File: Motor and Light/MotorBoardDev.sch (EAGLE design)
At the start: 79 parts, among them IC1 74HC04D, J1 Under Glow, J2 Safety Light, J3 12V, J4 24V, Q1 BC846ASMD, Q2 220mA/50V/3.5Ω, Q7 220mA/50V/3.5Ω, Q8 220mA/50V/3.5Ω, Q9 220mA/50V/3.5Ω, T11 TIP41A, T12 TIP41A, T13 TIP41A, T14 TIP41A, T15 TIP41A, T16 TIP41A, T17 TIP41A, T18 TIP41A, T19 TIP41A, T2 TIP41A, U2 9DoF IMU, X1 C-GRID-05-15-91, X2 C-GRID-05-15-91, X4 C-GRID-02-70553, X5 SI-50170, X7 2510-, X8 2510-

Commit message: added mbed pin maps
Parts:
- added R39, R40: 150, rcl:R-US_R0603
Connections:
- removed net VCC: X1-4.S, X2-4.S
- new net N$37: R39.1, U$15.P$30
- new net N$38: R40.1, U$15.P$29
- net +3V3: now also U2.!CS
- net +5V: now also X1-4.S, X2-4.S
- net 1S1: now also U$15.P$28
- net 1S2: now also U$15.P$27
- net 1S3: now also U$15.P$26
- net 2S1: now also U$15.P$5
- net 2S2: now also U$15.P$6
- net 2S3: now also U$15.P$7
- net BATTIN: now also U$15.P$20
- net ETH_LED1: now also R39.2
- net ETH_LED2: now also R40.2
- net GND: now also U2.FSYNC
- net GYRO_INT: now also U$15.P$14
- net LDIR: now also U$15.P$17
- net LEA3: now also U$15.P$24
- net LEB3: now also U$15.P$23
- net LSPEED: now also U$15.P$18
- net RDIR: now also U$15.P$15
- net REA3: now also U$15.P$22
- net REB3: now also U$15.P$21
- net RSPEED: now also U$15.P$16
- net SLIGHT: now also U$15.P$25

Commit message: added regulators
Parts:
- added C11, C12, C13, C14: (no value), rcl:C-USC0805
- added C6: 0.1uF, rcl:C-USC0603
- added U$7: NCP1117DT50GOS-ND, IGVC-Regulators:NCP1117DT50GOS-ND
- added U$8: NCP1117DT33GOS-ND, IGVC-Regulators:NCP1117DT33GOS-ND
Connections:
- net +12V: now also C11.1, C13.1, U$7.IN, U$8.IN
- net +3V3: now also C14.1, U$8.OUT
- net +5V: now also C12.1, C6.1, U$15.P$2, U$7.OUT
- net GND: now also C11.2, C12.2, C13.2, C14.2, C6.2, U$7.GND, U$8.GND

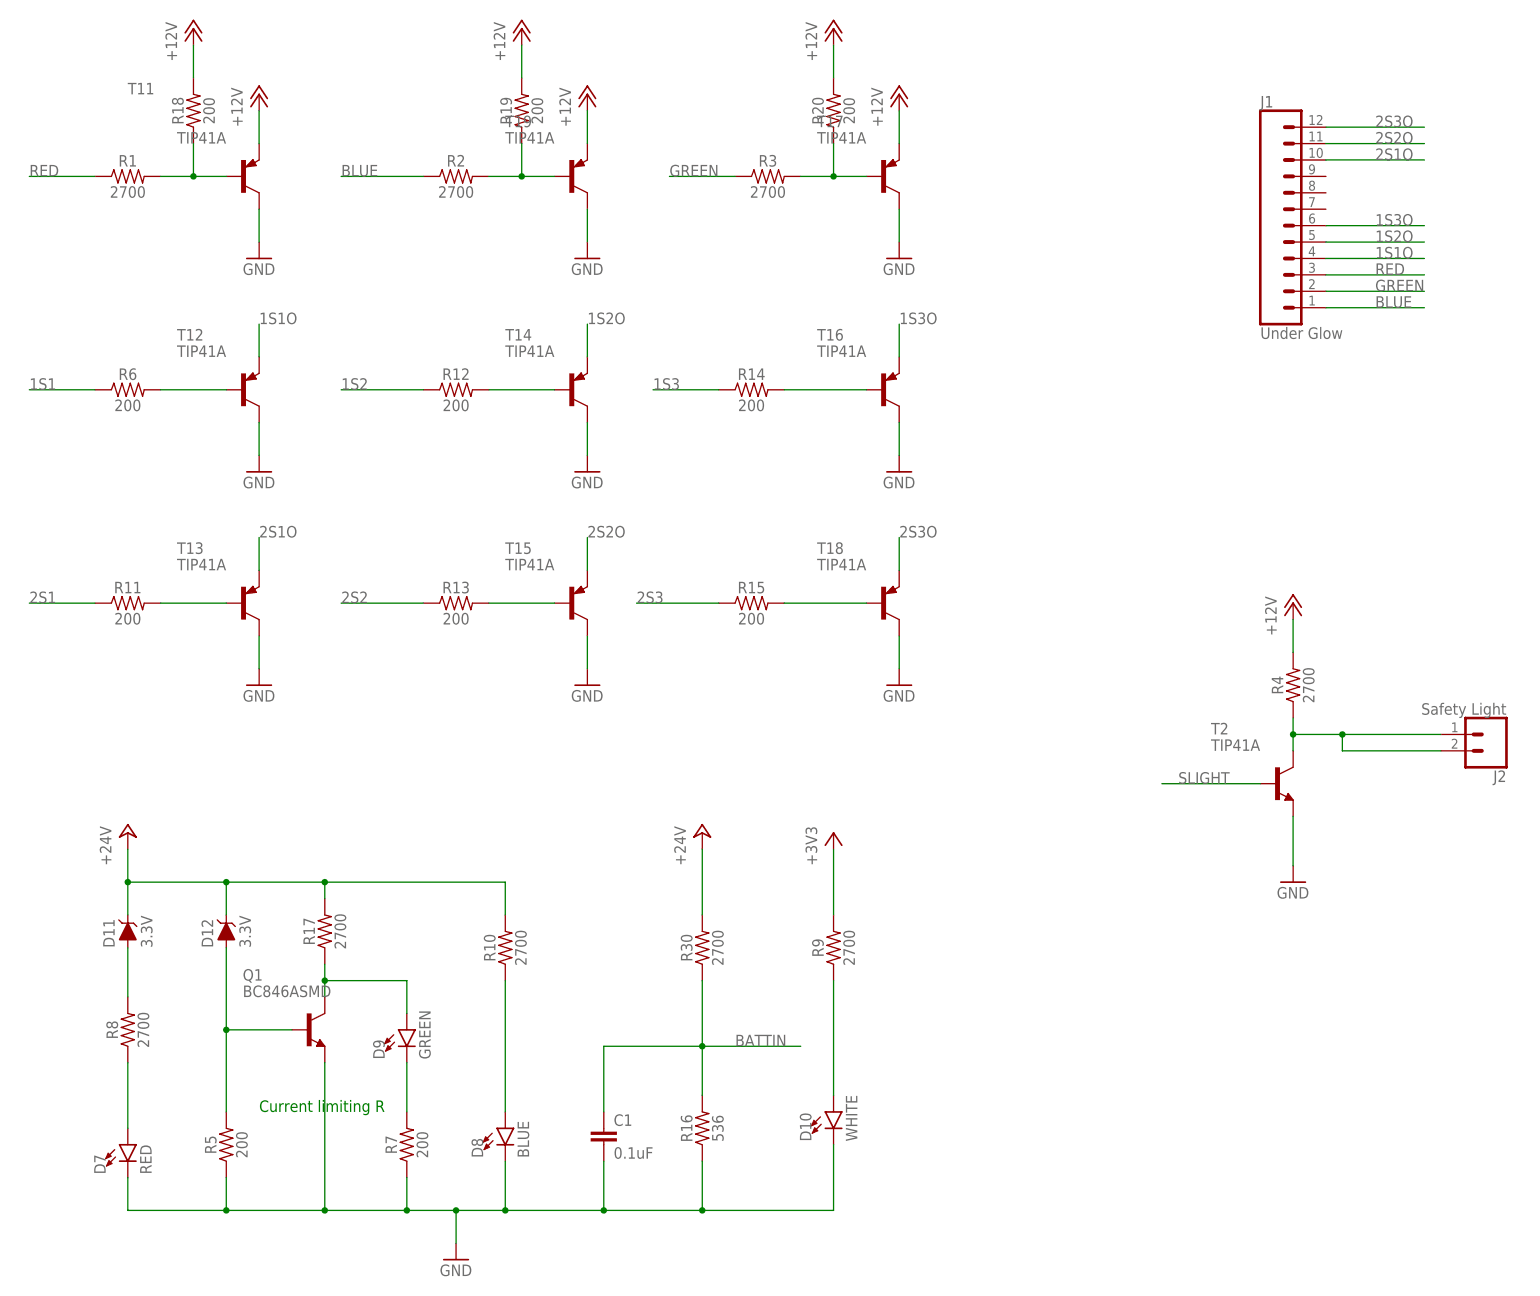
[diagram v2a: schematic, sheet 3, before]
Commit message: Schematics Updated, Layout initial commit
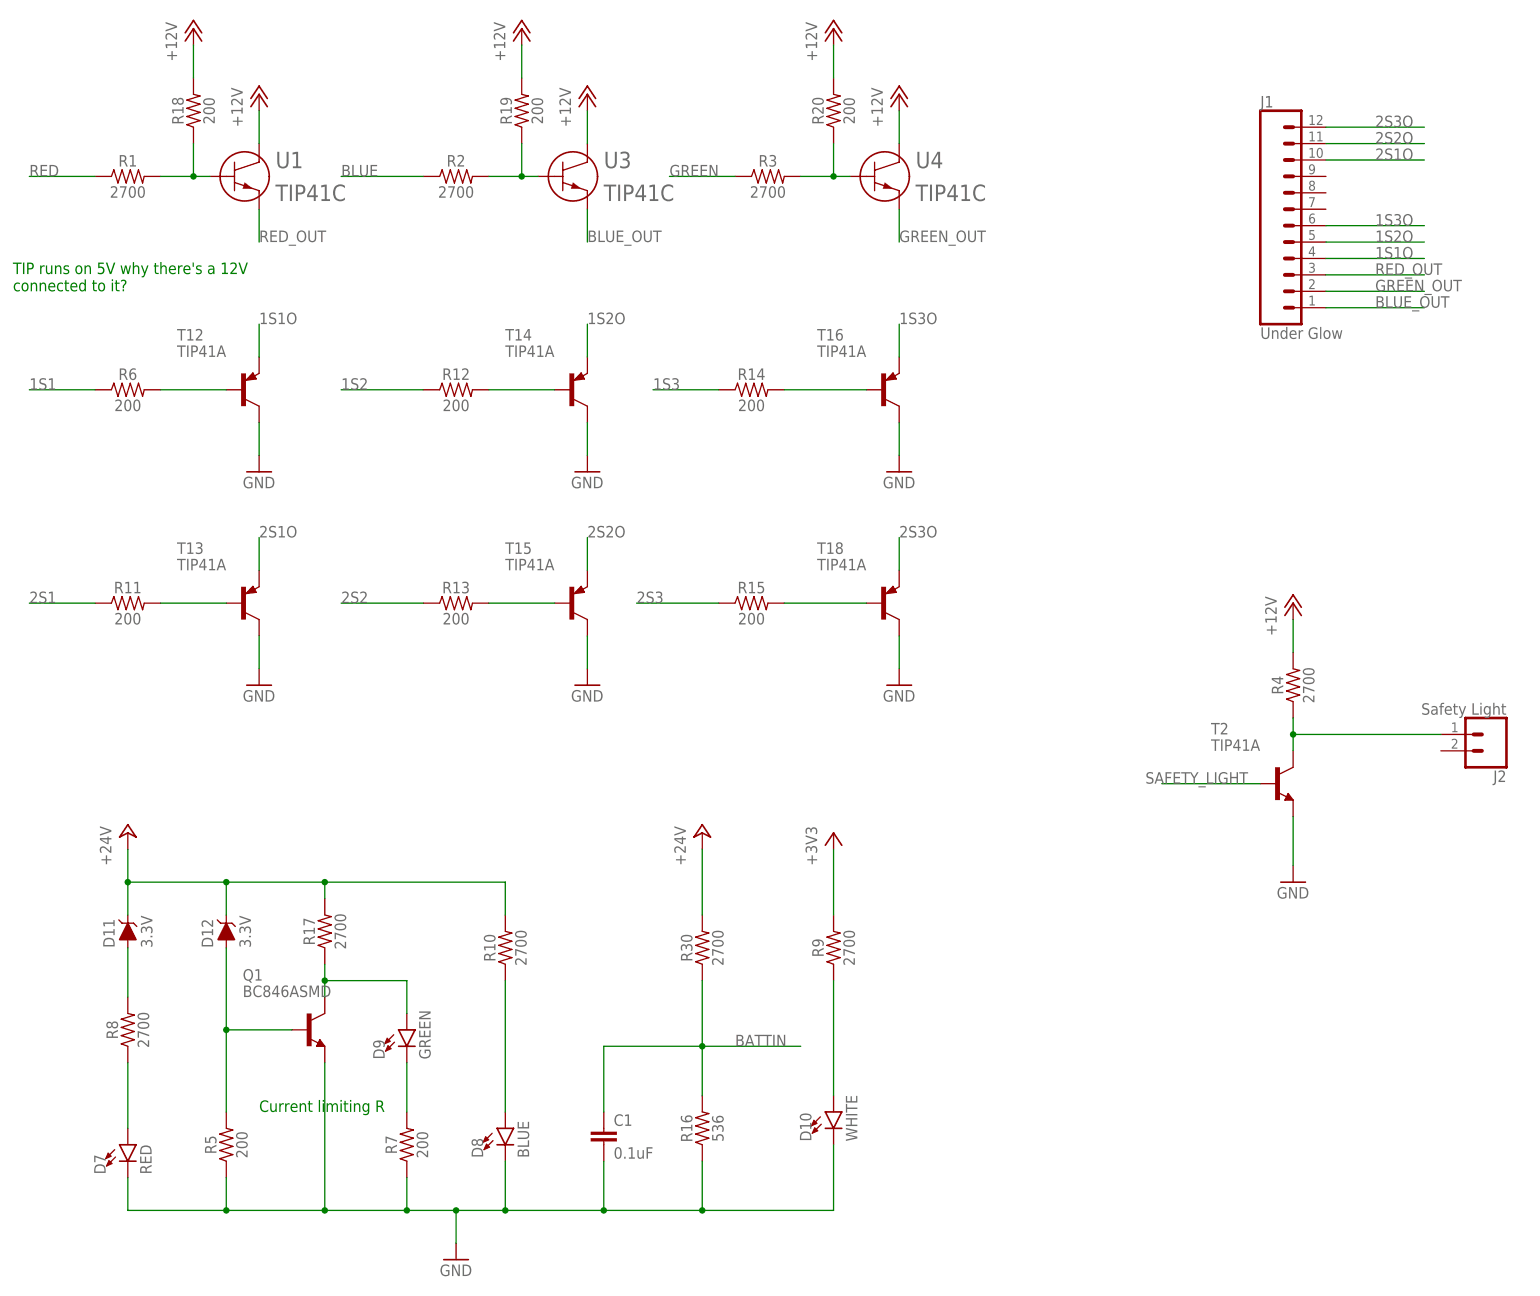
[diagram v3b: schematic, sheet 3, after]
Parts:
- removed T11, T17, T19: TIP41A, transistor:-PNP-TO220V
- added U1, U3, U4: TIP41C, DigiKey:TIP41C
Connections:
- net SLIGHT renamed SAFETY_LIGHT
- new net BLUE_OUT: J1.1, U3.E3
- new net GREEN_OUT: J1.2, U4.E3
- new net RED_OUT: J1.3, U1.E3
- net +12V: now also U1.C2, U3.C2, U4.C2; no longer T11.E, T17.E, T19.E
- net +3V3: now also U$15.P$40
- net BLUE: now also U$15.P$12; no longer J1.1
- net GND: no longer T11.C, T17.C, T19.C
- net GREEN: now also U$15.P$13; no longer J1.2
- net LDIR: now also IC1A.I; no longer IC1C.I
- net N$1: no longer J2.2
- net N$10: now also U4.B1; no longer T17.B
- net N$3: now also U1.B1; no longer T11.B
- net N$4: now also U3.B1; no longer T19.B
- net RDIR: now also IC1C.I; no longer IC1B.I
- net RED: now also U$15.P$11; no longer J1.3
- net RSPEED: now also IC1B.I; no longer IC1A.I
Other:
- note added: "TIP runs on 5V why there's a 12V connected to it?"

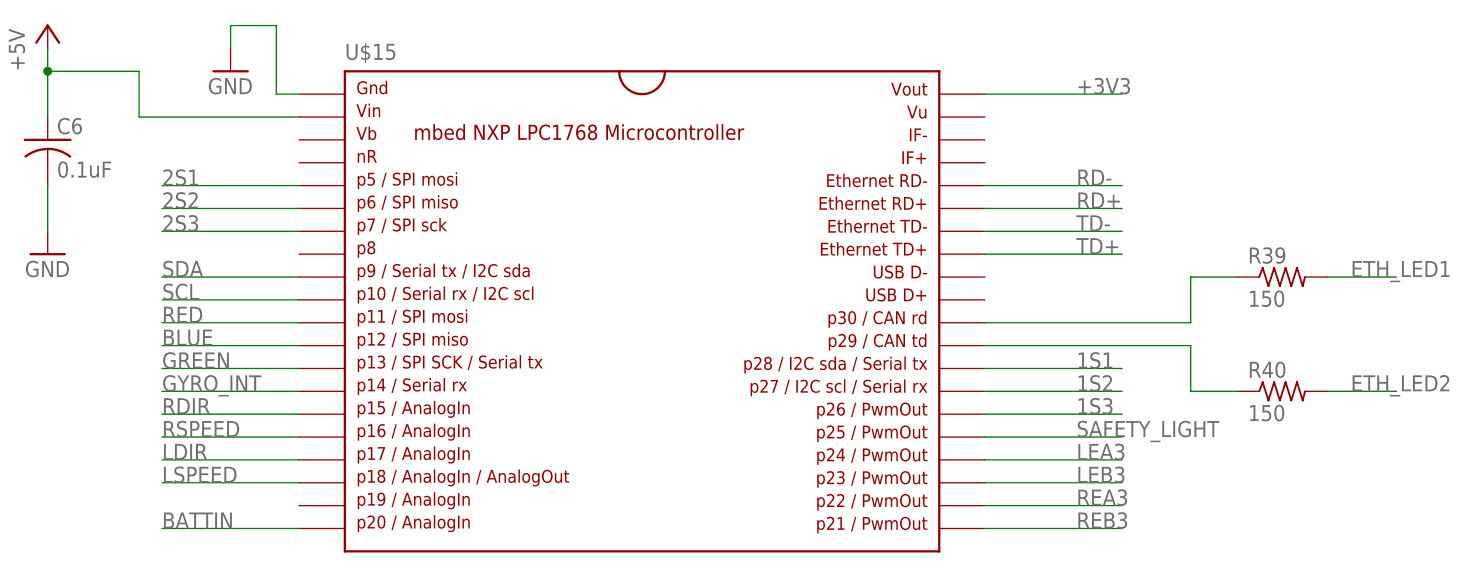
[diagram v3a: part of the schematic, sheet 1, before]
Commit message: Primary Layout Complete
Layout Complete, Sorting through Libraries
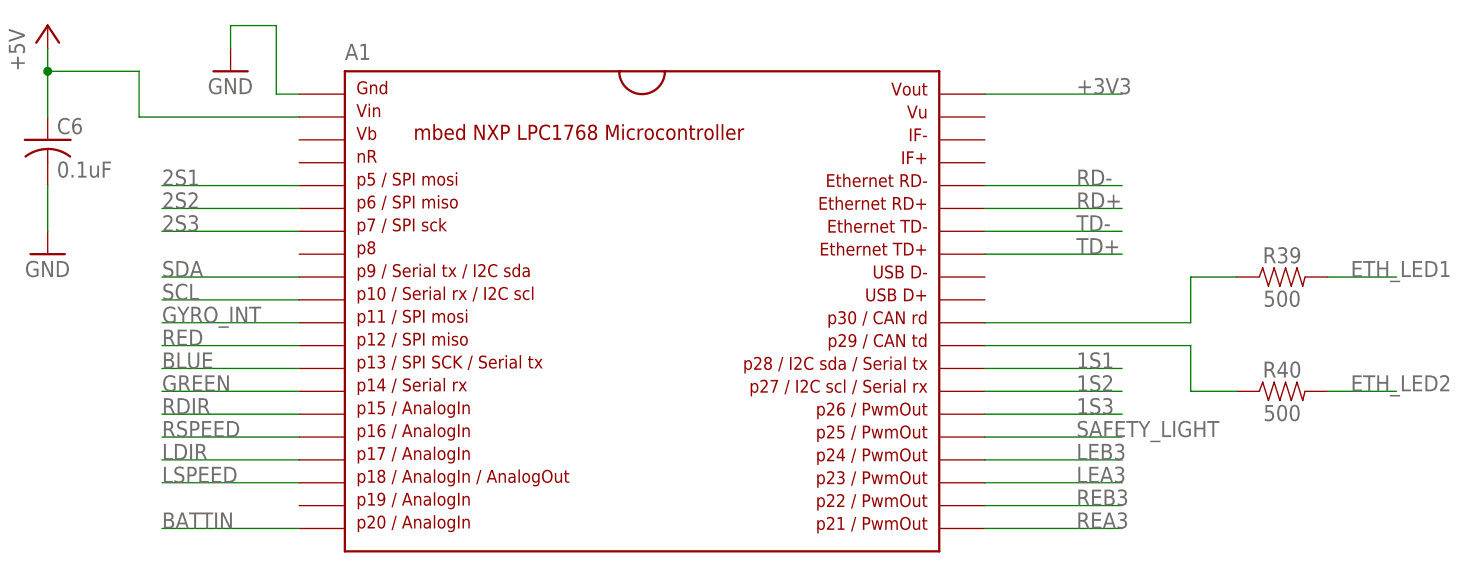
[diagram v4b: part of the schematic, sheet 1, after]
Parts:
- removed U$15: MBED1768, SparkFun-Boards:MBED_NXP_LPC1768
- added A1: MBED1768, MotorBoardDev:SPARKFUN-BOARDS_MBED_NXP_LPC1768
- R39, R40: value 150 -> 500; device rcl:R-US_R0603 -> SparkFun-Resistors:1KOHM-0603-1/10W-1%
- renumbered U$7 to T1, U$8 to T3, U1 to T5, U3 to T6, U4 to T7
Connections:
- net +3V3: now also A1.P$40; no longer U$15.P$40
- net +5V: now also A1.P$2; no longer U$15.P$2
- net 1S1: now also A1.P$28; no longer U$15.P$28
- net 1S2: now also A1.P$27; no longer U$15.P$27
- net 1S3: now also A1.P$26; no longer U$15.P$26
- net 2S1: now also A1.P$5; no longer U$15.P$5
- net 2S2: now also A1.P$6; no longer U$15.P$6
- net 2S3: now also A1.P$7; no longer U$15.P$7
- net BATTIN: now also A1.P$20; no longer U$15.P$20
- net BLUE: now also A1.P$13; no longer U$15.P$12
- net GND: now also A1.P$1; no longer U$15.P$1
- net GREEN: now also A1.P$14; no longer U$15.P$13
- net GYRO_INT: now also A1.P$11; no longer U$15.P$14
- net LDIR: now also A1.P$17; no longer U$15.P$17
- net LEA3: now also A1.P$23; no longer U$15.P$24
- net LEB3: now also A1.P$24; no longer U$15.P$23
- net LSPEED: now also A1.P$18; no longer U$15.P$18
- net N$37: now also A1.P$30; no longer U$15.P$30
- net N$38: now also A1.P$29; no longer U$15.P$29
- net RD+: now also A1.P$35; no longer U$15.P$35
- net RD-: now also A1.P$36; no longer U$15.P$36
- net RDIR: now also A1.P$15; no longer U$15.P$15
- net REA3: now also A1.P$21; no longer U$15.P$22
- net REB3: now also A1.P$22; no longer U$15.P$21
- net RED: now also A1.P$12; no longer U$15.P$11
- net RSPEED: now also A1.P$16; no longer U$15.P$16
- net SAFETY_LIGHT: now also A1.P$25; no longer U$15.P$25
- net SCL: now also A1.P$10; no longer U$15.P$10
- net SDA: now also A1.P$9; no longer U$15.P$9
- net TD+: now also A1.P$33; no longer U$15.P$33
- net TD-: now also A1.P$34; no longer U$15.P$34

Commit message: Updated Schematics Commit
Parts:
- removed D10: WHITE, SparkFun-LED:LED0603
- removed D11, D12: 3.3V, SparkFun-DiscreteSemi:DIODE-ZENER-MM3Z3V3T1G
- removed D7: RED, SparkFun-LED:LED0603
- removed D8: BLUE, SparkFun-LED:LED0603
- removed D9: GREEN, SparkFun-LED:LED0603
- removed IC1: 74HC04D, 74xx-eu:74HC04D
- removed R18, R19, R20: 200, SparkFun-Resistors:200OHM-0603-1/10W-1%
- removed R26, R30: 2700, SparkFun-Resistors:3.9KOHM-0603-1/10W-1%
- removed T12, T13, T14, T15, T16, T18: TIP41A, transistor:-PNP-TO220V
- removed T5, T6, T7: TIP41C, DigiKey:TIP41C
- added C7, C8: 10uF, rcl:C-USC0805
- added D1, D2: GREEN, SparkFun-LED:LED-GREEN0603
- added D3: WHITE, SparkFun-LED:LED-WHITE0603
- added D4: BLUE, SparkFun-LED:LED-BLUE0603
- added FQP30N06L, Q15, Q16: TIP41C, transistor-power:TIP41C
- added Q10, Q11, Q3, Q4, Q5, Q6: TIP42C, transistor-power:TIP42C
- added X3: MINI-USB_SHIELD5P4-32005-400, con-cypressindustries:MINI-USB_SHIELD5P4-32005-400
- C1: device SparkFun-Capacitors:0.1UF-0603-25V-(+80/-20%) -> SparkFun-Capacitors:0.1UF-0603-100V-10%
- C11, C12, C13, C14: value (none) -> 10uF
- Q1: value BC846ASMD -> TIP42C; device transistor-npn:BC846ASMD -> transistor-power:TIP42C
- R10: value 2700 -> 200; device SparkFun-Resistors:3.9KOHM-0603-1/10W-1% -> SparkFun-Resistors:200OHM-0603-1/10W-1%
- R16: value 536 -> 200; device SparkFun-Resistors:3.9KOHM-0603-1/10W-1% -> SparkFun-Resistors:200OHM-0603-1/10W-1%
- R7: value 200 -> 50
- R8: value 2700 -> 1800; device SparkFun-Resistors:3.9KOHM-0603-1/10W-1% -> SparkFun-Resistors:200OHM-0603-1/10W-1%
- R9: value 2700 -> 1000; device SparkFun-Resistors:3.9KOHM-0603-1/10W-1% -> SparkFun-Resistors:200OHM-0603-1/10W-1%
- T2: device transistor:-NPN-TO220V -> transistor:-PNP-TO220V
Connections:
- removed net !LDIR!: IC1C.O, R23.1
- removed net !LSPEED!: IC1D.O, R21.1
- removed net !RDIR!: IC1B.O, R24.1
- removed net !RSPEED!: IC1A.O, R22.1
- removed net N$24: D9.A, Q1.C, R17.1
- removed net N$33: D9.C, R7.2
- removed net N$34: D8.A, R10.1
- removed net N$35: D10.A, R9.1
- removed net N$7: D7.A, R8.1
- new net D+: A1.P$31, X3G$1.3
- new net D-: A1.P$32, X3G$1.2
- new net ID: X3G$1.4
- new net INDICATOR_LED: A1.P$8
- new net N$12: D4.A, R9.1
- new net N$5: D1.A, R5.1
- new net N$8: Q11.E, R17.1, X4-1.S
- net +12V: now also C7.1, FQP30N06L.C, Q15.C, Q16.C, R17.2, R9.2; no longer R18.2, R19.2, R20.2, T5.C2, T6.C2, T7.C2
- net +24V: now also C8.1, R8.2; no longer D11.C, D12.C, R17.2, R30.2
- net +3V3: now also R7.2; no longer R9.2
- net +5V: now also A1.P$39, R5.2, X3G$1.1; no longer IC1P.VCC
- net 1S1: now also A1.P$16; no longer A1.P$28
- net 1S1O: now also J1.7, Q1.E; no longer J1.4, T12.E
- net 1S2: now also A1.P$17; no longer A1.P$27
- net 1S2O: now also J1.6, Q4.E; no longer J1.5, T14.E
- net 1S3: now also A1.P$18; no longer A1.P$26
- net 1S3O: now also J1.5, Q6.E; no longer J1.6, T16.E
- net 2S1O: now also Q3.E; no longer T13.E
- net 2S2O: now also Q5.E; no longer T15.E
- net 2S3O: now also Q10.E; no longer T18.E
- net BATTIN: now also R10.1; no longer R30.1
- net BLUE: now also A1.P$21; no longer A1.P$13
- net BLUE_OUT: now also Q15.E; no longer T6.E3
- net ESTOP: now also A1.P$24, Q11.B; no longer R26.2, X4-1.S, X4-2.S
- net GND: now also C7.2, C8.2, D1.C, D2.C, D3.C, D4.C, J1.4, J1.8, J1.9, J2.2, Q1.C, Q10.C, Q11.C, Q3.C, Q4.C, Q5.C, Q6.C, T2.C, X3G$1.5, X4-2.S; no longer D10.C, D7.C, D8.C, IC1P.GND, Q1.E, R26.1, R5.1, R7.1, T12.C, T13.C, T14.C, T15.C, T16.C, T18.C, T2.E
- net GREEN: now also A1.P$22; no longer A1.P$14
- net GREEN_OUT: now also Q16.E; no longer T7.E3
- net L+12V: now also R28.2; no longer OK3A.COL, OK3B.COL, R28.1
- net LALI: now also OK3A.COL
- net LBLI: now also OK3B.COL, R28.1; no longer R28.2
- net LDIR: now also A1.P$26, R23.1; no longer A1.P$17, IC1A.I
- net LEA3: now also A1.P$13; no longer A1.P$23
- net LEB3: now also A1.P$12; no longer A1.P$24
- net LSPEED: now also A1.P$25, R21.1; no longer A1.P$18, IC1D.I
- net N$1: now also T2.E; no longer T2.C
- net N$10: now also Q16.B; no longer R20.1, T7.B1
- net N$11: now also Q6.B; no longer T16.B
- net N$13: now also Q4.B; no longer T14.B
- net N$14: now also Q1.B; no longer T12.B
- net N$15: now also Q3.B; no longer T13.B
- net N$16: now also Q5.B; no longer T15.B
- net N$28: now also Q10.B; no longer T18.B
- net N$3: now also FQP30N06L.B; no longer R18.1, T5.B1
- net N$4: now also Q15.B; no longer R19.1, T6.B1
- net N$6: now also D2.A, R7.1; no longer D11.A, R8.2
- net N$9: now also D3.A, R8.1; no longer D12.A, Q1.B, R5.2
- net R+12V: now also R25.2, R27.2; no longer OK4A.COL, OK4B.COL, R25.1, R27.1
- net RALI: now also OK4A.COL, R27.1; no longer R27.2
- net RBLI: now also OK4B.COL, R25.1; no longer R25.2
- net RDIR: now also A1.P$28, R24.1; no longer A1.P$15, IC1C.I
- net REA3: now also A1.P$15; no longer A1.P$21
- net REB3: now also A1.P$14; no longer A1.P$22
- net RED: now also A1.P$23; no longer A1.P$12
- net RED_OUT: now also FQP30N06L.E; no longer T5.E3
- net RSPEED: now also A1.P$27, R22.1; no longer A1.P$16, IC1B.I
- net SAFETY_LIGHT: now also A1.P$19; no longer A1.P$25
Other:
- note added: "Also logical shifters"
- note added: "Change to AZ2940D-3.3 for assurance over power supply"
- note added: "Change to AZ2940D-5.0 for assurance over power supply"
- note added: "FQP27P06"
- note added: "How it works?"
- note added: "I'll update the package when I get the chance, they look exactly in physical layout and schematics tho"
- note added: "I'll update this when I get the chance to make the library"
- note added: "I'm not sure how 1S1O/2S1O stuff works, but I've made then at least looks functional"
- note added: "ID set to floating to identify the board as a slave"
- note added: "Inverter removed, meaning writing 255 will actually cause 0 and the other way around will cause full speed"
- note added: "Look into this"
- note added: "Overkill?"
- note added: "RGB control pin underglow thrown to PWM"
- note added: "The following are P-Channel Logic Level Mosfet, FQP27P06"
- note added: "The inverter is gone"
- note added: "These are actual logic level mosfet that can run on 3.3V, parts number: FQP30N06L"
- note added: "This is a software problem!!"
- note added: "This transistor will be FQP27P06 as well"
- note added: "Will be a connector with horizontal pinout, JST B2PS-VH"
- note added: "all of Speed control thrown to PWM"
- note added: "pull up resistor position changed, it'll no longer short L/R+12V to L/R GND"
- note removed: "Current limiting R"
- note removed: "Inverter Power"
- note removed: "Inverters"
- note removed: "TIP runs on 5V why there's a 12V connected to it?"
- moved on the sheet: C1, C11, C12, C13, C14, C2, C3, C5, C6, J4, OK3A, OK3B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

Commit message: Layout Initial Commit
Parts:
- removed C7, C8: 10uF, rcl:C-USC0805
- added R18, R19: 4.7k, SparkFun-Resistors:4.7KOHM-0603-1/10W-1%
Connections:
- net +12V: no longer C7.1
- net +24V: no longer C8.1
- net +3V3: now also R18.2, R19.2
- net 1S1: now also A1.P$18; no longer A1.P$16
- net 1S3: now also A1.P$16; no longer A1.P$18
- net 2S1: now also A1.P$7; no longer A1.P$5
- net 2S3: now also A1.P$5; no longer A1.P$7
- net GND: no longer C7.2, C8.2
- net LEA3: now also A1.P$14; no longer A1.P$13
- net LEB3: now also A1.P$15; no longer A1.P$12
- net REA3: now also A1.P$12; no longer A1.P$15
- net REB3: now also A1.P$13; no longer A1.P$14
- net SCL: now also R18.1
- net SDA: now also R19.1
